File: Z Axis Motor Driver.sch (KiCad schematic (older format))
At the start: 36 parts, among them J2 Motor Z, U2 TMC2209-LA

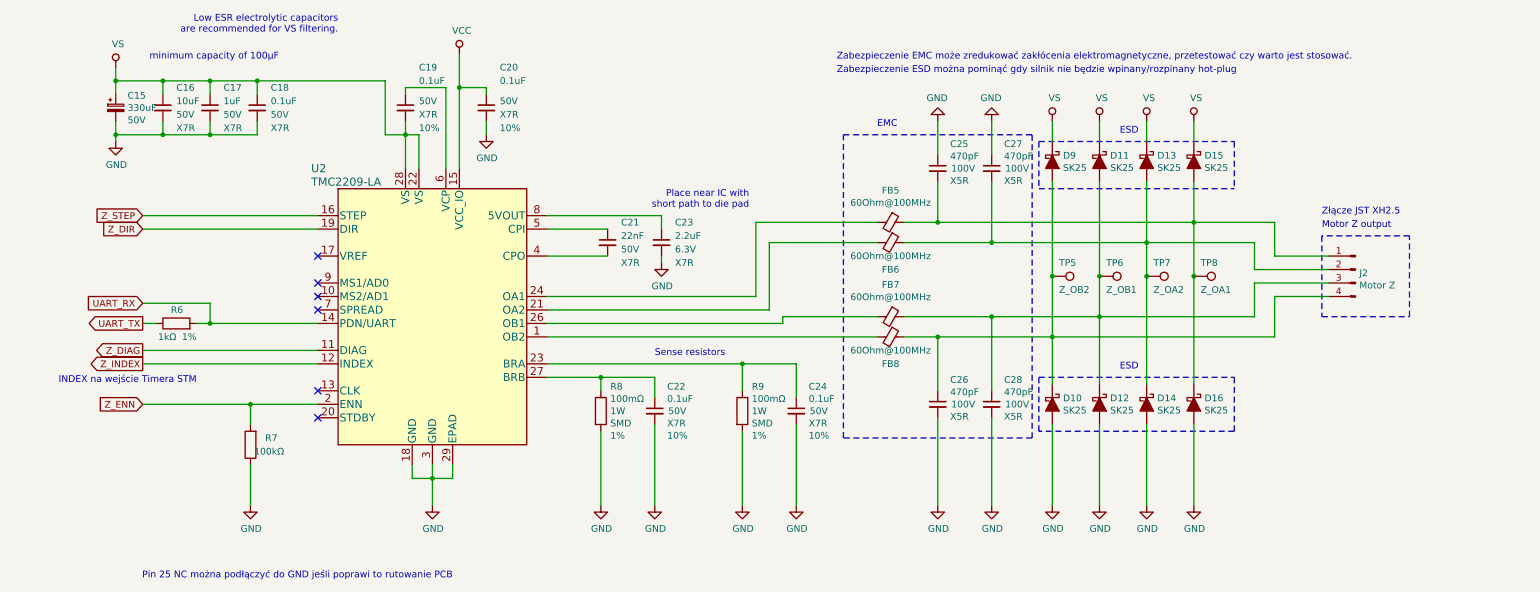
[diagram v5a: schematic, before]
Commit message: Added analog input
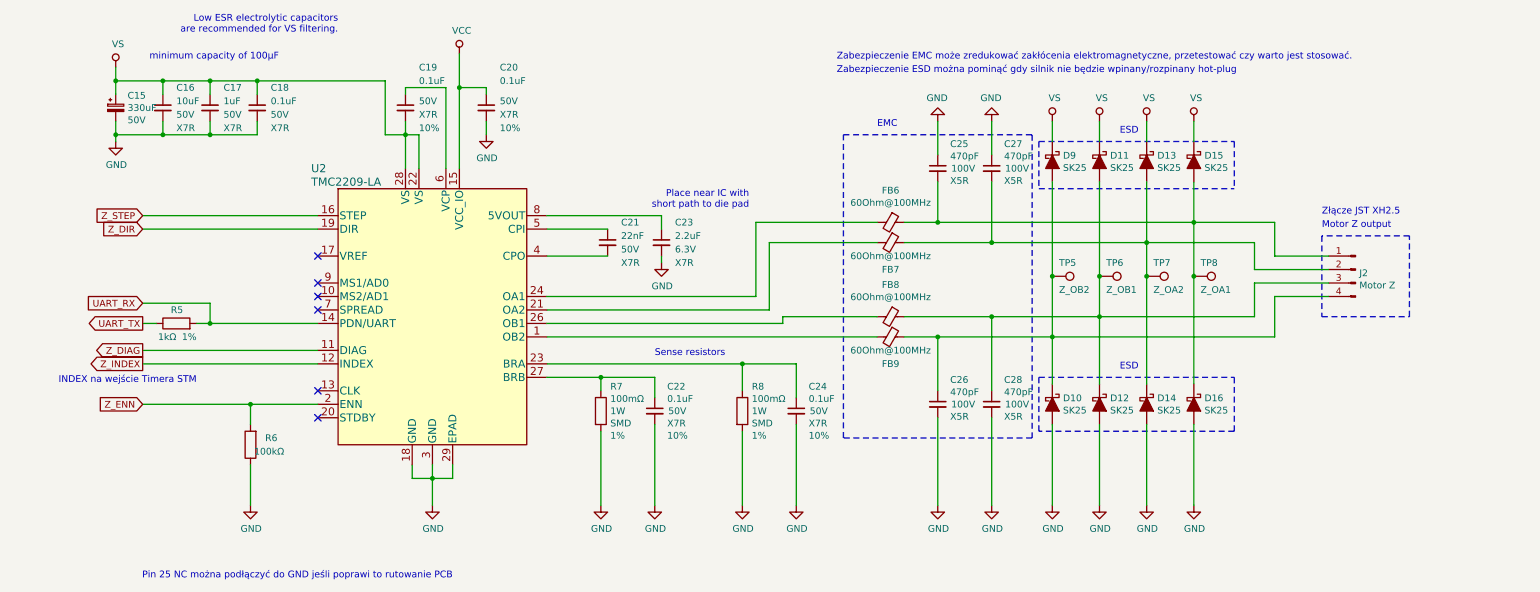
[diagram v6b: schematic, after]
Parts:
- renumbered FB5 to FB6, FB6 to FB7, FB7 to FB8, FB8 to FB9, R6 to R5, R7 to R6, R8 to R7, R9 to R8
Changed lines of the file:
@@
 $EndComp
 $Comp
-L Device:R R8
+L Device:R R7
 U 1 1 5DE71FB1
 P 4800 4300
-F 0 "R8" H 4870 4482 50  0000 L CNN
+F 0 "R7" H 4870 4482 50  0000 L CNN
 F 1 "100mΩ" H 4870 4391 50  0000 L CNN
 F 2 "Resistor_SMD:R_2010_5025Metric" V 4730 4300 50  0001 C CNN
@@
 $EndComp
 $Comp
-L Device:R R9
+L Device:R R8
 U 1 1 5DE7F13C
 P 5850 4300
-F 0 "R9" H 5920 4482 50  0000 L CNN
+F 0 "R8" H 5920 4482 50  0000 L CNN
 F 1 "100mΩ" H 5920 4391 50  0000 L CNN
 F 2 "Resistor_SMD:R_2010_5025Metric" V 5780 4300 50  0001 C CNN
@@
 	5850 4450 5850 5000
 $Comp
-L Device:Ferrite_Bead_Small FB5
+L Device:Ferrite_Bead_Small FB6
 U 1 1 5E01207D
 P 6950 2900
-F 0 "FB5" V 6713 2900 50  0000 C CNN
+F 0 "FB6" V 6713 2900 50  0000 C CNN
 F 1 "60Ohm@100MHz" V 6804 2900 50  0000 C CNN
 F 2 "Inductor_SMD:L_0805_2012Metric" V 6880 2900 50  0001 C CNN
@@
 $EndComp
 $Comp
-L Device:Ferrite_Bead_Small FB6
+L Device:Ferrite_Bead_Small FB7
 U 1 1 5E012E9C
 P 6950 3050
-F 0 "FB6" V 7150 3050 50  0000 C CNN
+F 0 "FB7" V 7150 3050 50  0000 C CNN
 F 1 "60Ohm@100MHz" V 7050 3050 50  0000 C CNN
 F 2 "Inductor_SMD:L_0805_2012Metric" V 6880 3050 50  0001 C CNN
@@
 $EndComp
 $Comp
-L Device:Ferrite_Bead_Small FB7
+L Device:Ferrite_Bead_Small FB8
 U 1 1 5E013189
 P 6950 3600
-F 0 "FB7" V 6713 3600 50  0000 C CNN
+F 0 "FB8" V 6713 3600 50  0000 C CNN
 F 1 "60Ohm@100MHz" V 6804 3600 50  0000 C CNN
 F 2 "Inductor_SMD:L_0805_2012Metric" V 6880 3600 50  0001 C CNN
@@
 $EndComp
 $Comp
-L Device:Ferrite_Bead_Small FB8
+L Device:Ferrite_Bead_Small FB9
 U 1 1 5E0133CC
 P 6950 3750
-F 0 "FB8" V 7150 3750 50  0000 C CNN
+F 0 "FB9" V 7150 3750 50  0000 C CNN
 F 1 "60Ohm@100MHz" V 7050 3750 50  0000 C CNN
 F 2 "Inductor_SMD:L_0805_2012Metric" V 6880 3750 50  0001 C CNN
@@
 UART_TX
 $Comp
-L Device:R R6
+L Device:R R5
 U 1 1 5E08CD42
 P 1650 3650
-F 0 "R6" V 1750 3600 50  0000 L CNN
+F 0 "R5" V 1750 3600 50  0000 L CNN
 F 1 "1kΩ" V 1550 3650 50  0000 L CNN
 F 2 "Resistor_SMD:R_0603_1608Metric" V 1580 3650 50  0001 C CNN
@@
 NoConn ~ 2700 4350
 $Comp
-L Device:R R7
+L Device:R R6
 U 1 1 5E21F7D5
 P 2200 4550
-F 0 "R7" H 2000 4500 50  0000 L CNN
+F 0 "R6" H 2000 4500 50  0000 L CNN
 F 1 "100kΩ" H 1950 4600 50  0000 L CNN
 F 2 "Resistor_SMD:R_0603_1608Metric" V 2130 4550 50  0001 C CNN

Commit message: Improve ESD Protection for TMC2209, Fuses. Schematic ready v1
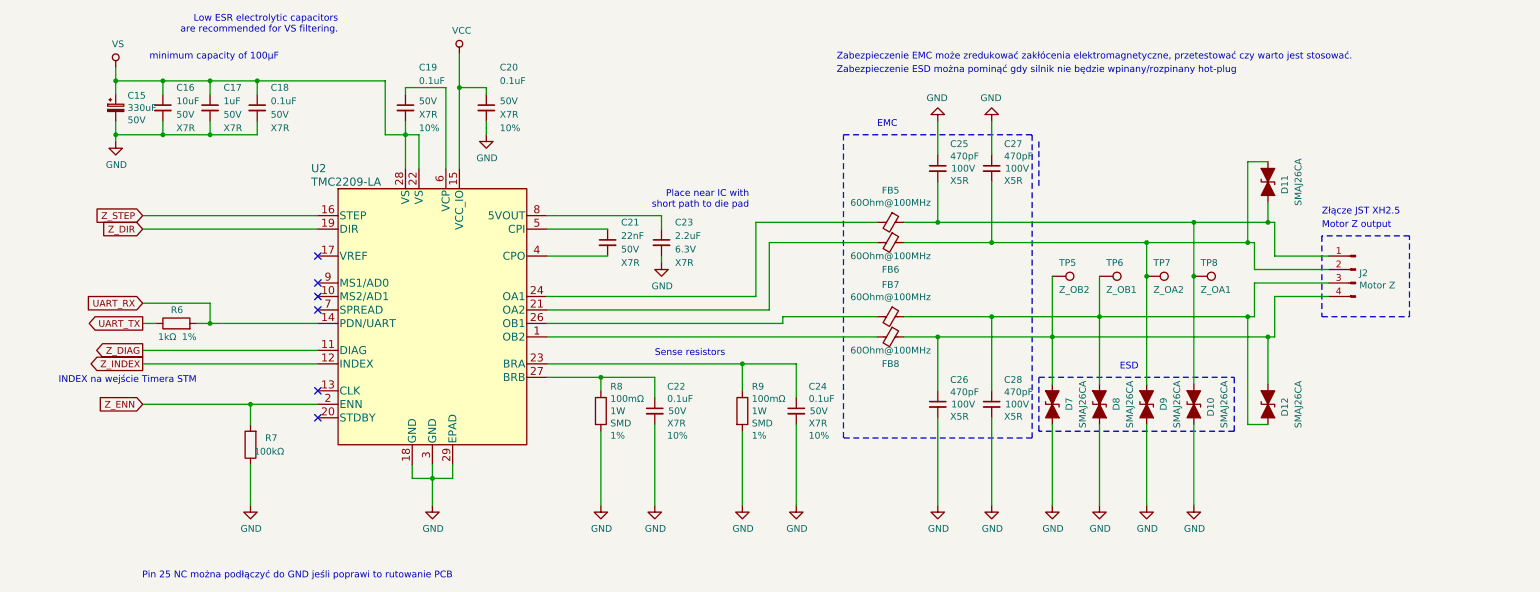
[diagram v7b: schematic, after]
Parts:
- removed D10, D11, D12, D13, D14, D15, D16, D9: SK25, Diode_SMD:D_SMB, symbol Device:D_Schottky_ALT
- added D10, D11, D12, D7, D8, D9: SMAJ26CA, Diode_SMD:D_SMA, symbol Device:D_TVS_ALT
- renumbered FB6 to FB5, FB7 to FB6, FB8 to FB7, FB9 to FB8, R5 to R6, R6 to R7, R7 to R8, R8 to R9
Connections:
- net GND: now also D10.2 (A2), D7.2 (A2), D8.2 (A2), D9.2 (A2)
- net at C25.2, FB5.1, J2.1 (Pin_1)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: now also D10.1 (A1), D11.2 (A2)
- net at C27.2, FB6.1, J2.2 (Pin_2)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: now also D11.1 (A1), D9.1 (A1)
- net at C28.1, FB7.1, J2.3 (Pin_3)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: now also D12.2 (A2), D8.1 (A1)
- net at C26.1, FB8.1, J2.4 (Pin_4)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: now also D12.1 (A1), D7.1 (A1)

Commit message: Routing emergnency, photo barier, relay, voltage detect, analog, footprint improvment
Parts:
- U2: footprint footprints:TMC2209-LA -> footprints:QFN-28_5X5_3X8_EPAD
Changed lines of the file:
@@
 F 0 "U2" H 2650 4700 60  0000 L CNN
 F 1 "TMC2209-LA" H 2650 4600 60  0000 L CNN
-F 2 "footprints:TMC2209-LA" V 3500 3600 60  0001 C CNN
+F 2 "footprints:QFN-28_5X5_3X8_EPAD" V 3500 3600 60  0001 C CNN
 F 3 "https://www.trinamic.com/fileadmin/assets/Products/ICs_Documents/TMC2209_Datasheet_V103.pdf" H 2500 4250 60  0001 C CNN
 F 4 "10.30" H 3550 3600 50  0001 C CNN "Cena"
